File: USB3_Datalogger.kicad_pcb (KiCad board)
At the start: 6 copper layers, 68.5 x 55 mm, 129 parts, among them J101 Conn_02x20_Odd_Even, J102 Conn_02x07_Odd_Even, J103 Conn_02x07_Odd_Even, J201 USB3-micro, J801 USB_B_Mini, J802 Conn_01x06, SW101 SW_Push, U101 ASDMB-xxxMHz, U201 FT600, U202 TPD2EUSB30, U203 TPD2EUSB30, U204 USB6B1, U301 ICE40HX1K-4K-TQ144, U303 INA226, U401 tps6240x, U402 TLV73325PDBV, U601 INA226, U701 INA226, U801 STM32F103RCTx, U802 USB6B1, U803 W25Q32JVZP, Y201 30MHz

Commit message: Last cleanups before PCB manufacturing
Signed-off-by: Alexis Jeandet <alexis.jeandet@member.fsf.org>
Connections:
- net /STM32/FLASH_CDONE renamed /FPGA/FLASH_CDONE
- net /STM32/FLASH_~CRESET renamed /FPGA/FLASH_~CRESET
- net /Sheet5E41F9C9/3.3V renamed /USB3/3.3V
- net /Sheet5E41F9C9/5VUSBMON/A0 renamed /USB3/5VUSBMON/A0
- net /Sheet5E41F9C9/5VUSBMON/A1 renamed /USB3/5VUSBMON/A1
- net /Sheet5E41F9C9/BE_0 renamed /USB3/BE_0
- net /Sheet5E41F9C9/BE_1 renamed /USB3/BE_1
- net /Sheet5E41F9C9/CLK renamed /USB3/CLK
- net /Sheet5E41F9C9/DATA_0 renamed /FPGA/DATA_0
- net /Sheet5E41F9C9/DATA_1 renamed /FPGA/DATA_1
- net /Sheet5E41F9C9/DATA_10 renamed /FPGA/DATA_10
- net /Sheet5E41F9C9/DATA_11 renamed /FPGA/DATA_11
- net /Sheet5E41F9C9/DATA_12 renamed /FPGA/DATA_12
- net /Sheet5E41F9C9/DATA_13 renamed /FPGA/DATA_13
- net /Sheet5E41F9C9/DATA_14 renamed /FPGA/DATA_14
- net /Sheet5E41F9C9/DATA_15 renamed /FPGA/DATA_15
- net /Sheet5E41F9C9/DATA_2 renamed /FPGA/DATA_2
- net /Sheet5E41F9C9/DATA_3 renamed /FPGA/DATA_3
- net /Sheet5E41F9C9/DATA_4 renamed /FPGA/DATA_4
- net /Sheet5E41F9C9/DATA_5 renamed /FPGA/DATA_5
- net /Sheet5E41F9C9/DATA_6 renamed /FPGA/DATA_6
- net /Sheet5E41F9C9/DATA_7 renamed /FPGA/DATA_7
- net /Sheet5E41F9C9/DATA_8 renamed /FPGA/DATA_8
- net /Sheet5E41F9C9/DATA_9 renamed /FPGA/DATA_9
- net /Sheet5E41F9C9/SSRX+ renamed /USB3/SSRX+
- net /Sheet5E41F9C9/SSRX- renamed /USB3/SSRX-
- net /Sheet5E41F9C9/SSTX+ renamed /USB3/SSTX+
- net /Sheet5E41F9C9/SSTX- renamed /USB3/SSTX-
- net /Sheet5E41F9C9/TOD+ renamed /USB3/TOD+
- net /Sheet5E41F9C9/TOD- renamed /USB3/TOD-
- net /Sheet5E41F9C9/USB2_D+ renamed /USB3/USB2_D+
- net /Sheet5E41F9C9/USB2_D- renamed /USB3/USB2_D-
- net /Sheet5E41F9C9/VBUS renamed /USB3/VBUS
- net /Sheet5E41F9C9/VD10 renamed /USB3/VD10
- net /Sheet5E4285EB/FIFO_GPIO_0 renamed /FPGA/FIFO_GPIO_0
- net /Sheet5E4285EB/FIFO_GPIO_1 renamed /FPGA/FIFO_GPIO_1
- net /Sheet5E4285EB/FLASH_CLK renamed /FPGA/FLASH_CLK
- net /Sheet5E4285EB/FLASH_MISO renamed /FPGA/FLASH_MISO
- net /Sheet5E4285EB/FLASH_MOSI renamed /FPGA/FLASH_MOSI
- net /Sheet5E4285EB/FLASH_SS renamed /FPGA/FLASH_SS
- net /Sheet5E4285EB/~FIFO_OE renamed /FPGA/~FIFO_OE
- net /Sheet5E4285EB/~FIFO_RD renamed /FPGA/~FIFO_RD
- net /Sheet5E4285EB/~FIFO_RXF renamed /FPGA/~FIFO_RXF
- net /Sheet5E4285EB/~FIFO_TXE renamed /FPGA/~FIFO_TXE
- net /Sheet5E4285EB/~FIFO_WR renamed /FPGA/~FIFO_WR
- net /Sheet5F0E3366/#1.2V renamed /Power/#1.2V
- net /Sheet5F0E3366/#3.3V renamed /Power/#3.3V
- net /Sheet5F0E3366/sheet5E682359/A0 renamed /Power/1V2Monitor/A0
- net /Sheet5F0E3366/sheet5E682359/A1 renamed /Power/1V2Monitor/A1
- net /Sheet5F0E3366/sheet5E682C33/A0 renamed /Power/3V3Monitor/A0
- net /Sheet5F0E3366/sheet5E682C33/A1 renamed /Power/3V3Monitor/A1
- J201 pad 4: Net-(J201-Pad4) -> (no net)
- J801 pad 4: Net-(J801-Pad4) -> (no net)
- J802 pad 1: Net-(J802-Pad1) -> (no net)
- J802 pad 4: Net-(J802-Pad4) -> (no net)
- U101 pad 1: Net-(U101-Pad1) -> (no net)
- U201 pad 11: Net-(U201-Pad11) -> (no net)
- U201 pad 14: Net-(U201-Pad14) -> (no net)
- U301 pad 109: Net-(U301-Pad109) -> (no net)
- U301 pad 110: Net-(U301-Pad110) -> (no net)
- U301 pad 124: Net-(U301-Pad124) -> (no net)
- U301 pad 125: Net-(U301-Pad125) -> (no net)
- U301 pad 130: Net-(U301-Pad130) -> (no net)
- U301 pad 15: Net-(U301-Pad15) -> (no net)
- U301 pad 16: Net-(U301-Pad16) -> (no net)
- U301 pad 17: Net-(U301-Pad17) -> (no net)
- U301 pad 18: Net-(U301-Pad18) -> (no net)
- U301 pad 28: /IOL_18 -> (no net)
- U301 pad 29: /IOL_19 -> (no net)
- U301 pad 37: /IOB_0 -> (no net)
- U301 pad 55: Net-(U301-Pad55) -> (no net)
- U301 pad 77: Net-(U301-Pad77) -> (no net)
- U301 pad 82: Net-(U301-Pad82) -> (no net)
- U301 pad 83: Net-(U301-Pad83) -> (no net)
- U301 pad 84: Net-(U301-Pad84) -> (no net)
- U301 pad 85: Net-(U301-Pad85) -> (no net)
- U303 pad 3: Net-(U303-Pad3) -> (no net)
- U402 pad 4: Net-(U402-Pad4) -> (no net)
- U601 pad 3: Net-(U601-Pad3) -> (no net)
- U701 pad 3: Net-(U701-Pad3) -> (no net)
- U801 pad 1: Net-(U801-Pad1) -> (no net)
- U801 pad 10: Net-(U801-Pad10) -> (no net)
- U801 pad 11: Net-(U801-Pad11) -> (no net)
- U801 pad 14: Net-(U801-Pad14) -> (no net)
- U801 pad 15: Net-(U801-Pad15) -> (no net)
- U801 pad 16: Net-(U801-Pad16) -> (no net)
- U801 pad 17: Net-(U801-Pad17) -> (no net)
- U801 pad 2: Net-(U801-Pad2) -> (no net)
- U801 pad 20: /STM32/SPI1_NSS -> (no net)
- U801 pad 24: Net-(U801-Pad24) -> (no net)
- U801 pad 25: Net-(U801-Pad25) -> (no net)
- U801 pad 26: Net-(U801-Pad26) -> (no net)
- U801 pad 27: Net-(U801-Pad27) -> (no net)
- U801 pad 28: Net-(U801-Pad28) -> (no net)
- U801 pad 3: Net-(U801-Pad3) -> (no net)
- U801 pad 37: Net-(U801-Pad37) -> (no net)
- U801 pad 38: Net-(U801-Pad38) -> (no net)
- U801 pad 39: Net-(U801-Pad39) -> (no net)
- U801 pad 4: Net-(U801-Pad4) -> (no net)
- U801 pad 40: Net-(U801-Pad40) -> (no net)
- U801 pad 41: Net-(U801-Pad41) -> (no net)
- U801 pad 42: Net-(U801-Pad42) -> (no net)
- U801 pad 43: Net-(U801-Pad43) -> (no net)
- U801 pad 5: Net-(U801-Pad5) -> (no net)
- U801 pad 6: Net-(U801-Pad6) -> (no net)
- U801 pad 61: Net-(U801-Pad61) -> (no net)
- U801 pad 62: Net-(U801-Pad62) -> (no net)
- U801 pad 8: Net-(U801-Pad8) -> (no net)
- U801 pad 9: Net-(U801-Pad9) -> (no net)
- Y201 pad 2: Net-(Y201-Pad2) -> (no net)
- Y201 pad 4: Net-(Y201-Pad4) -> (no net)
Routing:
- net GND: vias 86 -> 85

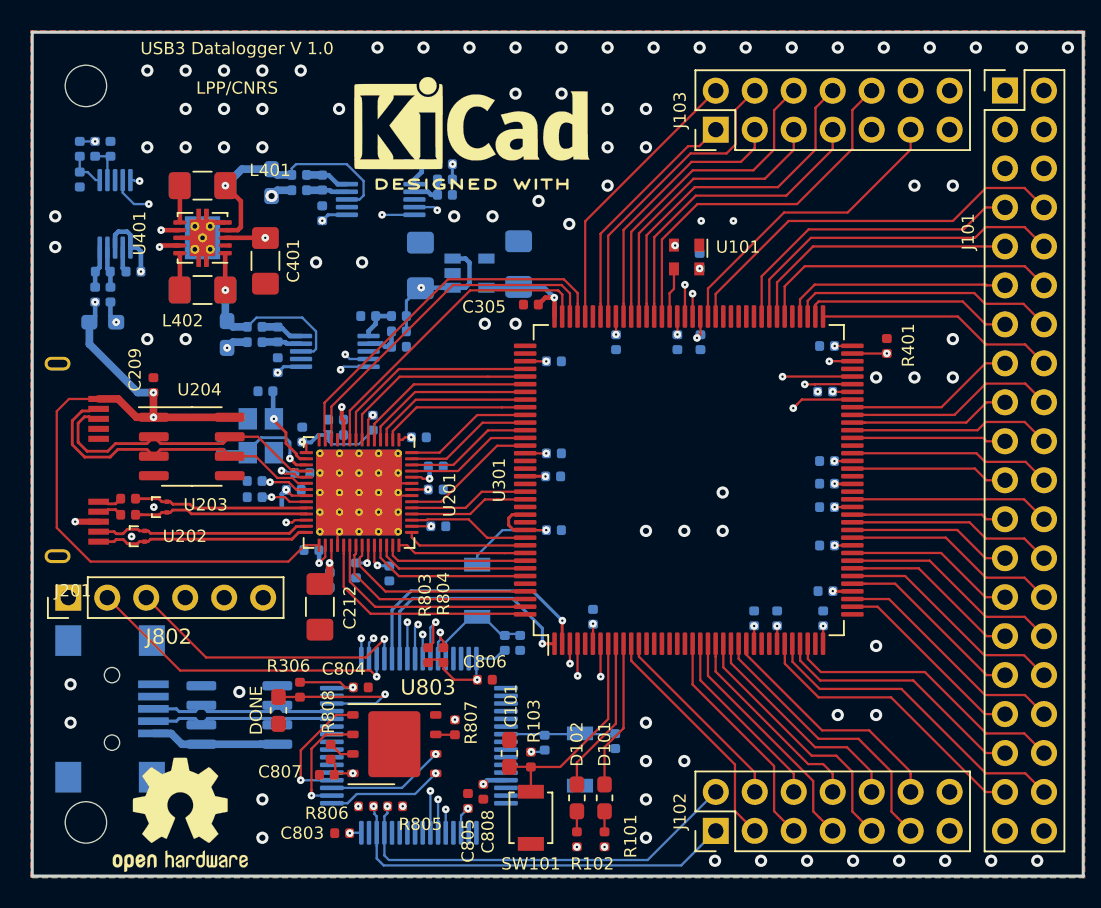
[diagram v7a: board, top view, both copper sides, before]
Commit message: Many fixes for 1.1
- fixed FTDI power supply mistake(3.3V was floating)
- updated resistors footprints
- updated push button footprints
- connected STM32 UART 1 to programming header
- added pull up resistor on USB D+ for STM32
- added 10uF capacitors on 5V and 3.3V near daughter board connectors

Signed-off-by: Alexis Jeandet <alexis.jeandet@member.fsf.org>
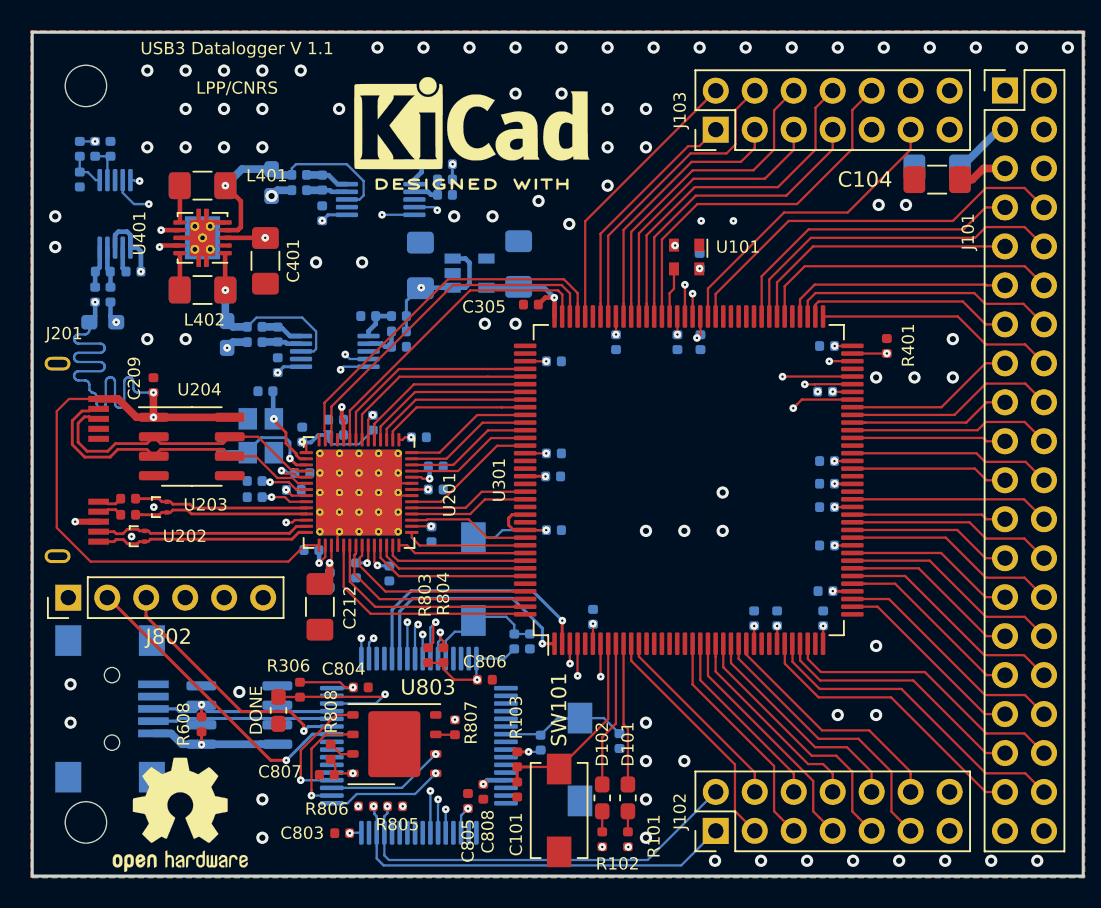
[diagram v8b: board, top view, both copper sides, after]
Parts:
- added C102: 10µF, Capacitor_SMD:C_1206_3216Metric_Pad1.42x1.75mm_HandSolder, B.Cu at (141.5, 148.8)
- added C104: 10µF, Capacitor_SMD:C_1206_3216Metric_Pad1.42x1.75mm_HandSolder, F.Cu at (141.5, 149.6)
- added R608: 4k7, Resistor_SMD:R_0402_1005Metric, F.Cu at (93.5, 185.1)
- BOOT0, RST0, SW101: footprint Button_Switch_SMD:SW_SPST_B3U-1000P -> Button_Switch_SMD:SW_SPST_EVQPE1
- C101: value C -> 100nF; footprint Capacitor_SMD:C_0603_1608Metric_Pad1.05x0.95mm_HandSolder -> Capacitor_SMD:C_0402_1005Metric
- C201, C202, C203, C204, C205, C207, C209, C210, C211, C213, C214, C215, C216, C801, C802: value C -> 100nF
- R201, R310, R311, R312, R313, R604, R605, R606, R607, R704, R705, R706, R707: footprint Capacitor_SMD:C_0402_1005Metric -> Resistor_SMD:R_0402_1005Metric
- moved C101 2.41 mm to (114.1, 189.4), turned to 270 degrees
- moved SW101 1.90 mm to (116.8, 190.7)
- moved D102 1.65 mm to (119.7, 189.9)
- moved R102 1.65 mm to (119.7, 192.6)
- moved D101 1.52 mm to (121.3, 189.9)
- moved R101 1.52 mm to (121.3, 192.6)
- moved R103 0.89 mm to (114.1, 187.4)
- moved BOOT0 0.80 mm to (111.3, 175.6)
- moved C203 0.68 mm to (108.5, 172.7), turned to 270 degrees
- moved R801 0.64 mm to (114.9, 179.7)
- moved C801 0.63 mm to (113.9, 179.7)
- moved C802 0.28 mm to (120.8, 186.2)
- moved R802 0.27 mm to (115.6, 186.3)
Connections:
- C201 pad 1: /USB3/3.3V -> VCCIO_0
- C202 pad 1: /USB3/3.3V -> VCCIO_0
- C203 pad 1: /USB3/3.3V -> VCCIO_0
- C204 pad 1: /USB3/3.3V -> VCCIO_0
- C205 pad 1: /USB3/3.3V -> VCCIO_0
- C207 pad 1: /USB3/3.3V -> VCCIO_0
- C210 pad 1: /USB3/3.3V -> VCCIO_0
- J802 pad 2: /STM32/UART4_TX -> /STM32/UART1_TX
- J802 pad 3: /STM32/UART4_RX -> /STM32/UART1_RX
- R202 pad 1: /USB3/3.3V -> VCCIO_0
- R203 pad 1: /USB3/3.3V -> VCCIO_0
- U201 pad 15: /USB3/3.3V -> VCCIO_0
- U201 pad 19: /USB3/3.3V -> VCCIO_0
- U201 pad 22: /USB3/3.3V -> VCCIO_0
- U201 pad 30: /USB3/3.3V -> VCCIO_0
- U201 pad 38: /USB3/3.3V -> VCCIO_0
- U201 pad 44: /USB3/3.3V -> VCCIO_0
- U201 pad 52: /USB3/3.3V -> VCCIO_0
- U801 pad 42: (no net) -> /STM32/UART1_TX
- U801 pad 43: (no net) -> /STM32/UART1_RX
- U801 pad 51: /STM32/UART4_TX -> (no net)
- U801 pad 52: /STM32/UART4_RX -> (no net)
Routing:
- net VCCIO_0: track 72.0 -> 101.7 mm, vias 24 -> 31
- net /STM32/UART4_TX: track 20.9 -> 0.00 mm, vias 1 -> 0
- net /STM32/UART1_TX: track 0.00 -> 19.7 mm, vias 0 -> 1
- net /USB3/3.3V: track 19.3 -> 0.00 mm, vias 7 -> 0
- net /STM32/UART4_RX: track 18.9 -> 0.00 mm, vias 1 -> 0
- net /USB3/VBUS: track 69.2 -> 86.1 mm
- net /STM32/UART1_RX: track 0.00 -> 16.8 mm, vias 0 -> 1
- net /USB_5V: track 133.4 -> 137.4 mm
- net /STM32/BOOT0: track 7.09 -> 8.34 mm
- net /STM32/RESET: track 7.12 -> 8.26 mm
- net /IOL_5: track 14.3 -> 13.1 mm
- net /STM32/VBUS: track 8.37 -> 9.28 mm, vias 0 -> 1
- net /STM32/USB_D+: track 12.4 -> 13.1 mm, vias 0 -> 1
- net /IOL_6: track 10.2 -> 9.54 mm
- added copper zone on In2.Cu, net VCCIO_0
- removed copper zone on In2.Cu, net /USB3/3.3V
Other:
- board text added: "USB3 Datalogger V 1.1 LPP/CNRS"
- board text removed: "USB3 Datalogger V 1.0 LPP/CNRS"
